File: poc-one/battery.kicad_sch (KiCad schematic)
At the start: 40 parts, among them J4 Connector, USB-TYPE-C-16P, Q4 2N7002, Q6 SS8550 Y2 200-350, SW3 BAT_SYS_PWR, U021 BQ24195LRGER, U2 NCP1117-3.3_SOT223

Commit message: poc-one update & bom
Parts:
- added R40: 1k5, Resistor_SMD:R_0402_1005Metric, symbol Device:R
- C1, C19, C22, C25, C26, C27, C5: footprint Capacitor_SMD:C_0805_2012Metric -> Capacitor_SMD:C_0402_1005Metric
- C23: footprint Capacitor_SMD:C_0805_2012Metric -> Capacitor_SMD:C_0603_1608Metric
- D18, D19, D20: footprint (none) -> LED_SMD:LED_0603_1608Metric
- L2: footprint (none) -> Inductor_SMD:L_0603_1608Metric
- R11, R17, R20, R32, R33, R35, R36, R37, R38, TH1: footprint (none) -> Resistor_SMD:R_0402_1005Metric
- R14: value 333 -> 220; footprint (none) -> Resistor_SMD:R_0402_1005Metric
- R34: value 5k49 -> 5k1; footprint (none) -> Resistor_SMD:R_0402_1005Metric
- SW3: value BAT_SYS_PWR -> BAT_SYS_PWR HY-DSIC02LS; footprint HY-DSIC02LS -> Button_Switch_SMD:SW_DIP_SPSTx02_Slide_9.78x7.26mm_W8.61mm_P2.54mm
- TP1: value TestPoint -> VBUS; footprint (none) -> TestPoint:TestPoint_Pad_D1.5mm
- TP2: value TestPoint -> +3V8 / VSYS; footprint (none) -> TestPoint:TestPoint_Pad_D1.5mm
- TP3, TP7: footprint (none) -> TestPoint:TestPoint_Pad_D1.5mm
- TP4: value TestPoint -> +3V3; footprint (none) -> TestPoint:TestPoint_Pad_D1.5mm
- TP5: value TestPoint -> +1V1; footprint (none) -> TestPoint:TestPoint_Pad_D1.5mm
- TP6: value TestPoint -> GND; footprint (none) -> TestPoint:TestPoint_Pad_D1.5mm
- U021: footprint (none) -> Package_DFN_QFN:VQFN-24-1EP_4x4mm_P0.5mm_EP2.45x2.45mm
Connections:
- net at R37.1, TH1.1, U021.11 (TS1)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: now also R40.2; no longer R34.2
- new net: R34.2, R40.1
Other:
- note added: "V_LTF < V_TS < V_HTF to start V_LTF < V_TS < V_TCO while on V_LTF = 73.5% of REGN V_HTF = 47.2% of REGN V_TCO = 44.7% of REGN currently: 6.6k / 10k => 66% of REGN constant"
- note added: "todo: replace and calculate actual thermistor"
- note removed: "todo: calculate thermistor"
- moved on the sheet: R34, TP1, TP2, TP4, TP5

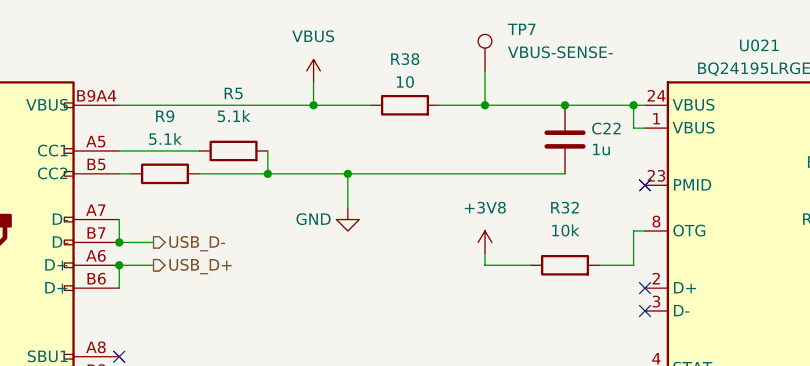
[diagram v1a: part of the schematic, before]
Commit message: fixed a couple resistors, reworked footprints incl. datasheets
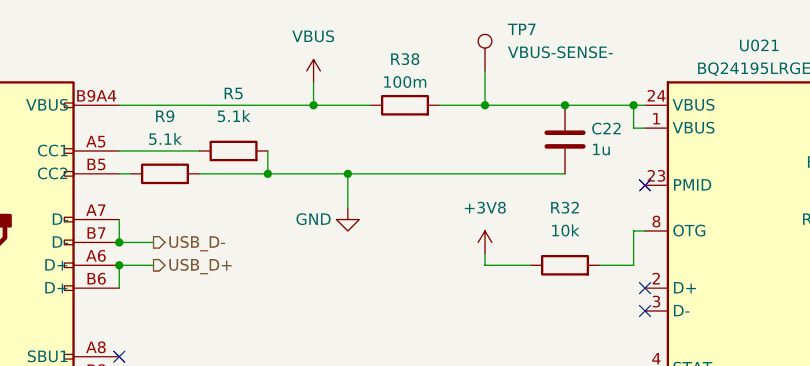
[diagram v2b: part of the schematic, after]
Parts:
- R38: value 10 -> 100m; footprint Resistor_SMD:R_0402_1005Metric -> Resistor_SMD:R_1206_3216Metric
- TP1, TP2, TP3, TP4, TP5, TP6, TP7: now left out of the parts list
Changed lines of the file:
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@@
 		(body_style 1)
 		(exclude_from_sim no)
-		(in_bom yes)
+		(in_bom no)
 		(on_board yes)
-		(in_pos_files yes)
+		(in_pos_files no)
 		(dnp no)
 		(fields_autoplaced yes)
@@
 		(body_style 1)
 		(exclude_from_sim no)
-		(in_bom yes)
+		(in_bom no)
 		(on_board yes)
-		(in_pos_files yes)
+		(in_pos_files no)
 		(dnp no)
 		(fields_autoplaced yes)
@@
 		(body_style 1)
 		(exclude_from_sim no)
-		(in_bom yes)
+		(in_bom no)
 		(on_board yes)
-		(in_pos_files yes)
+		(in_pos_files no)
 		(dnp no)
 		(fields_autoplaced yes)
@@
 			)
 		)
-		(property "Value" "10"
+		(property "Value" "100m"
 			(at 72.39 41.91 90)
 			(show_name no)
@@
 			)
 		)
-		(property "Footprint" "Resistor_SMD:R_0402_1005Metric"
+		(property "Footprint" "Resistor_SMD:R_1206_3216Metric"
 			(at 72.39 46.228 90)
 			(hide yes)
@@
 		(body_style 1)
 		(exclude_from_sim no)
-		(in_bom yes)
+		(in_bom no)
 		(on_board yes)
-		(in_pos_files yes)
+		(in_pos_files no)
 		(dnp no)
 		(fields_autoplaced yes)
@@
 		(body_style 1)
 		(exclude_from_sim no)
-		(in_bom yes)
+		(in_bom no)
 		(on_board yes)
-		(in_pos_files yes)
+		(in_pos_files no)
 		(dnp no)
 		(fields_autoplaced yes)
@@
 		(body_style 1)
 		(exclude_from_sim no)
-		(in_bom yes)
+		(in_bom no)
 		(on_board yes)
-		(in_pos_files yes)
+		(in_pos_files no)
 		(dnp no)
 		(fields_autoplaced yes)
@@
 		(body_style 1)
 		(exclude_from_sim no)
-		(in_bom yes)
+		(in_bom no)
 		(on_board yes)
-		(in_pos_files yes)
+		(in_pos_files no)
 		(dnp no)
 		(fields_autoplaced yes)

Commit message: poc-one routed & schematic changes
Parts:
- C22: renamed from C25; value 4u7 -> 4.7u
- R19: renamed from R34; value 5k1 -> 5.1k
- R20: renamed from R40; value 1k5 -> 1.5k
- TH1: now left out of the parts list
- renumbered C22 to C19, C23 to C20, C19 to C21, C26 to C23, C27 to C24, C1 to C25, C5 to C26, D20 to D1, D19 to D2, D18 to D3, J4 to J3, Q6 to Q1, Q4 to Q2, R35 to R10, R9 to R11, R5 to R12, R11 to R13, R38 to R14, R32 to R15, R33 to R16, R37 to R17, R14 to R18, R17 to R21, R20 to R22, R36 to R9, TP4 to TP3, TP7 to TP4, TP3 to TP7, U021 to U3, U2 to U4
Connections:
- net GND: now also U3.25 (Thermal); no longer U3. (Thermal)
- net at C21.1, SW3.2, TP7.1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: no longer Q1.2 (E)
- net at BT1.1 (+), SW3.3: now also Q1.2 (E)
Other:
- note added: "TODO: replace with fully SMD mount connector (?) C2927040"
- moved on the sheet: BT1, TP7
